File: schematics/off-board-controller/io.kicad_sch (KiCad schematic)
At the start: 6 parts, among them SW5 SW_SPDT_MSM, SW6 SW_Push, SW7 SW_Push, SW8 SW_Push, U7 CA56-12EWA

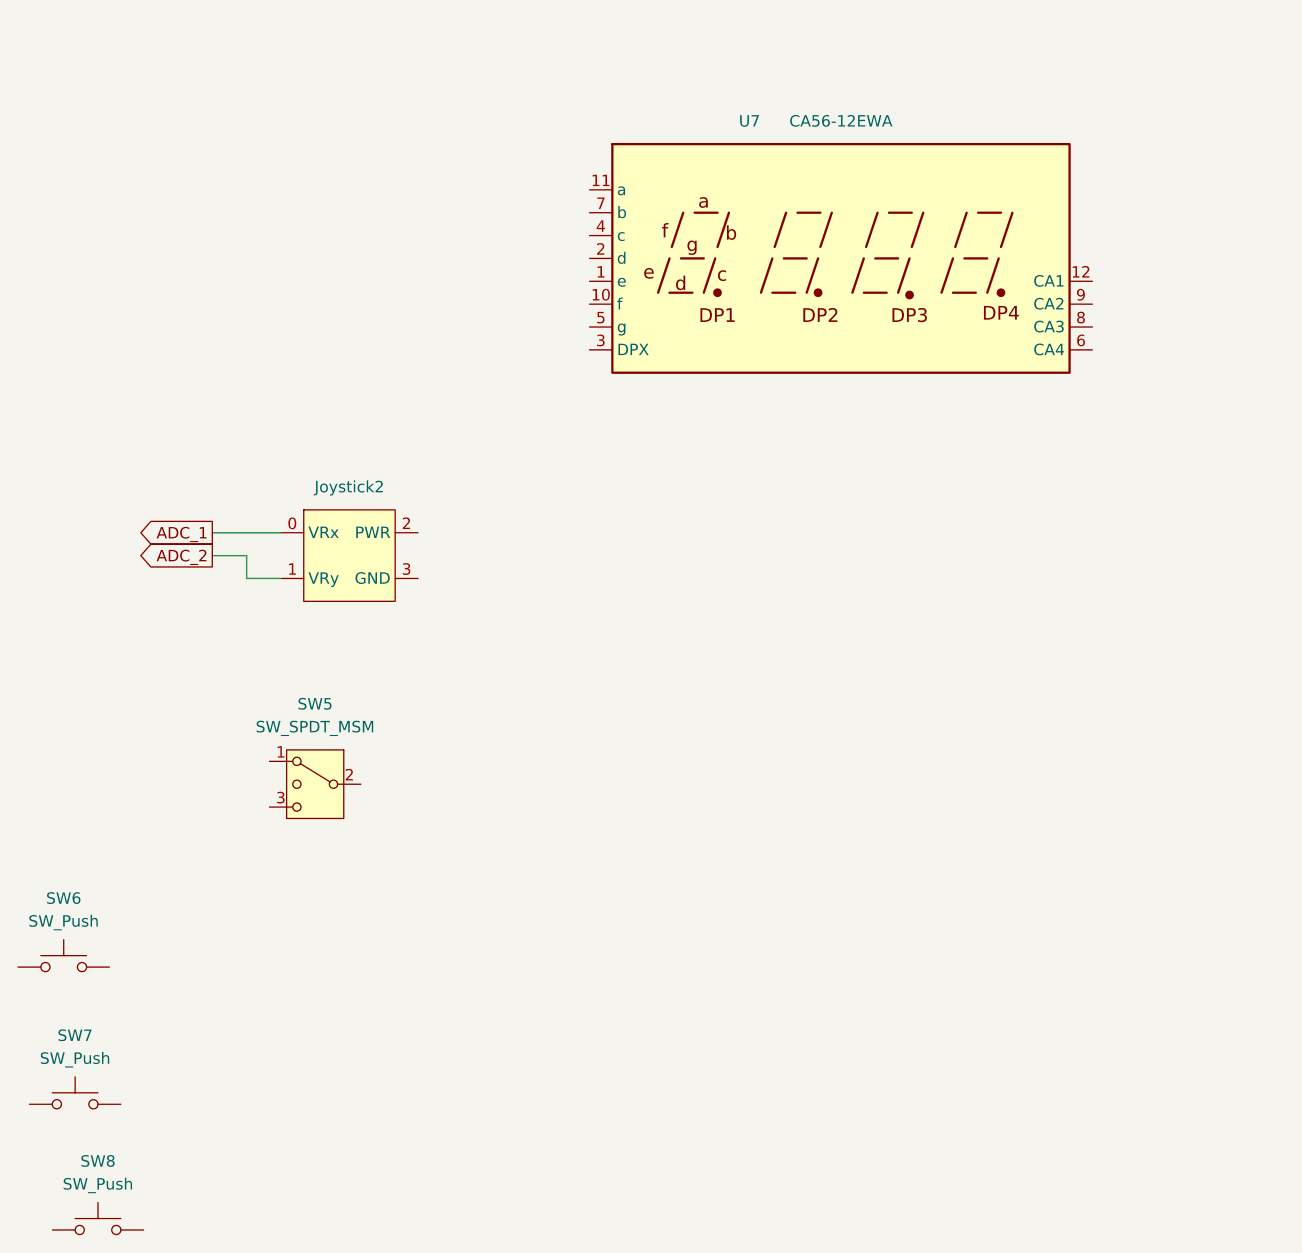
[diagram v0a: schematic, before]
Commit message: off-board: created schematic
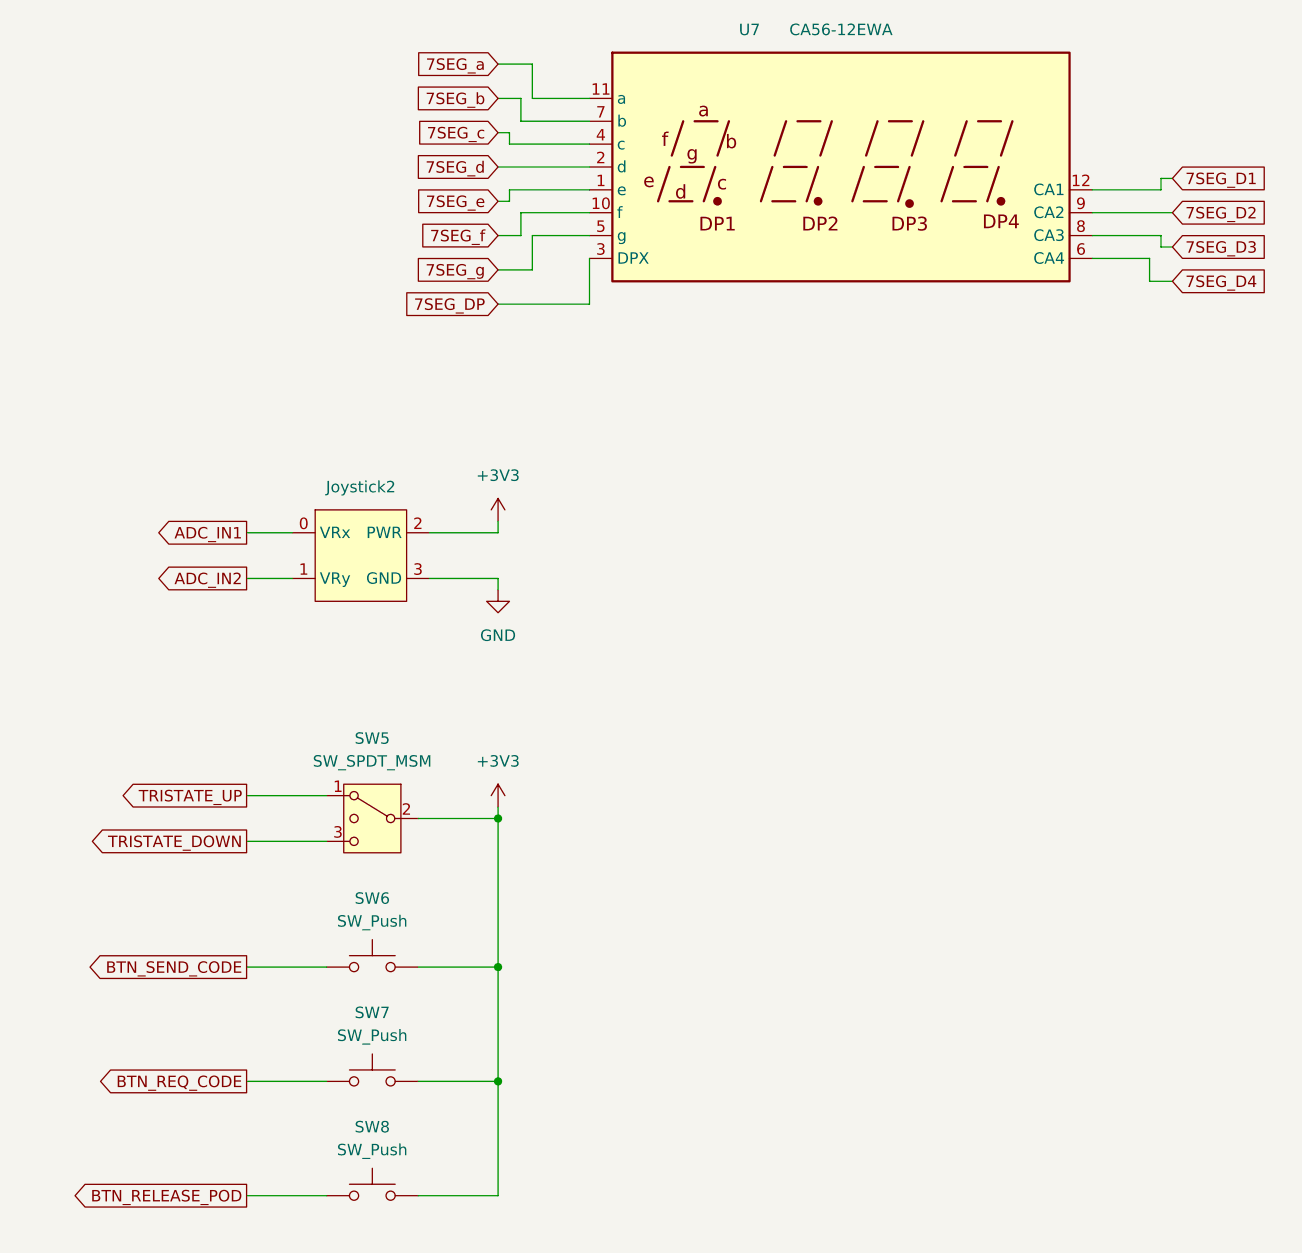
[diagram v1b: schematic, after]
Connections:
- net BTN_REQ_CODE: now reaches SW7.1
- net +3V3: now reaches SW7.2
- net +3V3: now also Joystick2.2 (PWR), SW5.2 (3), SW6.2, SW8.2
- net 7SEG_e: now reaches U7.1 (e)
- net 7SEG_f: now reaches U7.10 (f)
- net 7SEG_a: now reaches U7.11 (a)
- net 7SEG_D1: now reaches U7.12 (CA1)
- net 7SEG_d: now reaches U7.2 (d)
- net 7SEG_DP: now reaches U7.3 (DPX)
- net 7SEG_c: now reaches U7.4 (c)
- net 7SEG_g: now reaches U7.5 (g)
- net 7SEG_D4: now reaches U7.6 (CA4)
- net 7SEG_b: now reaches U7.7 (b)
- net 7SEG_D3: now reaches U7.8 (CA3)
- net 7SEG_D2: now reaches U7.9 (CA2)
- net BTN_RELEASE_POD: now reaches SW8.1
- net TRISTATE_UP: now reaches SW5.1
- net TRISTATE_DOWN: now reaches SW5.3 (4)
- net BTN_SEND_CODE: now reaches SW6.1
- net GND: now reaches Joystick2.3 (GND)
- net ADC_1 renamed ADC_IN1
- net ADC_2 renamed ADC_IN2
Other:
- title: (none) -> Off-board Controller
- moved on the sheet: Joystick2, SW5, SW6, SW7, SW8, U7

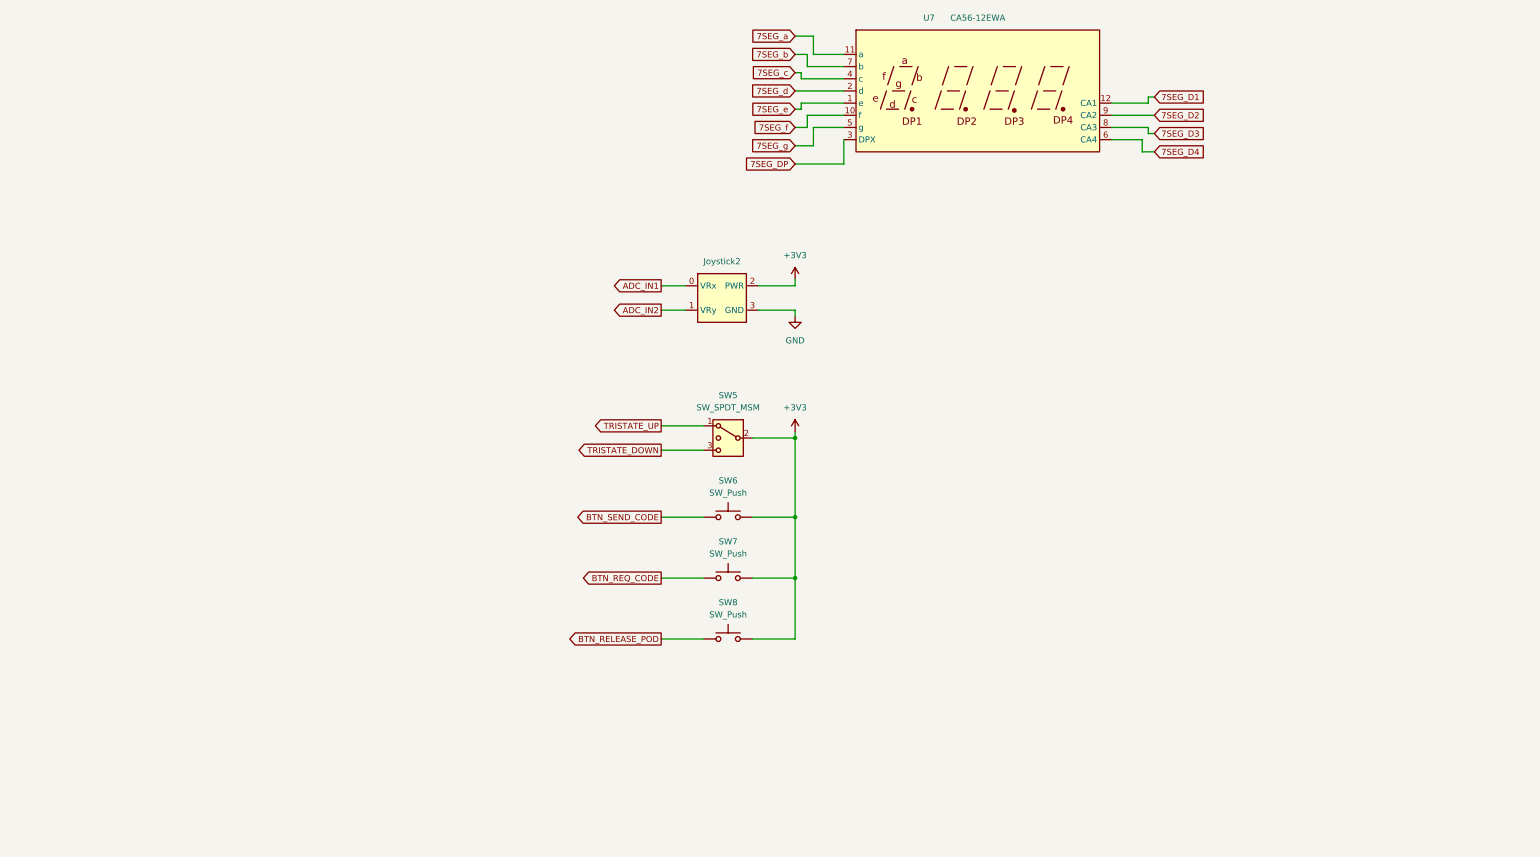
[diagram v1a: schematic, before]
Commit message: finished footprints, schematic, and started layout
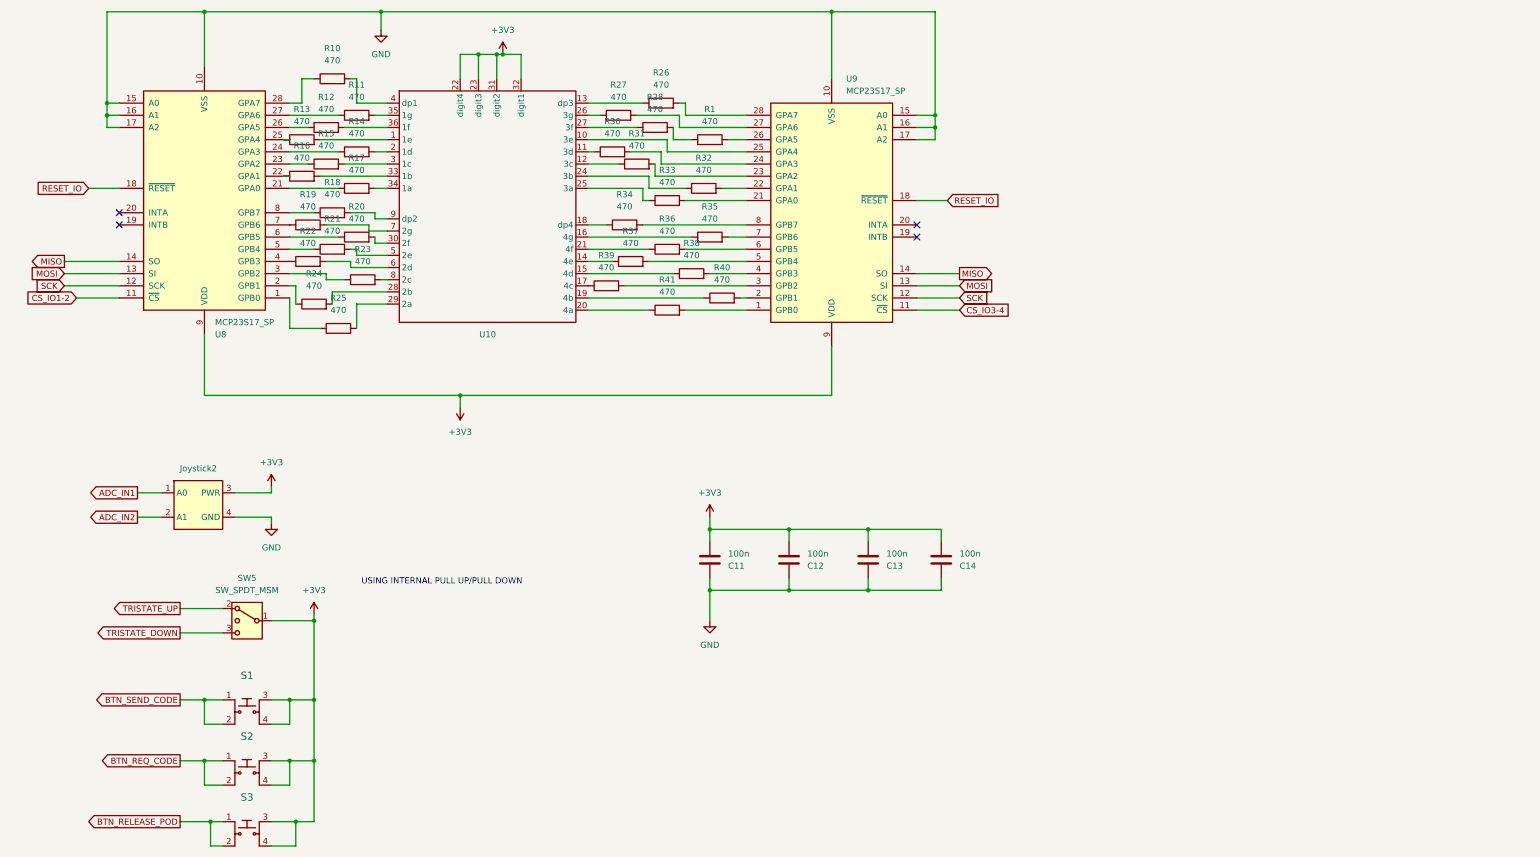
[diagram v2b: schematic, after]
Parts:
- removed SW6, SW7, SW8: SW_Push, symbol Switch:SW_Push
- removed U7: CA56-12EWA, Display_7Segment:CA56-12EWA, symbol Display_Character:CA56-12EWA
- added C11, C12, C13, C14: 100n, Capacitor_SMD:C_0805_2012Metric_Pad1.18x1.45mm_HandSolder, symbol Device:C
- added R1, R10, R11, R12, R13, R14, R15, R16, R17, R18, R19, R20, R21, R22, R23, R24, R25, R26, R27, R28, R30, R31, R32, R33, R34, R35, R36, R37, R38, R39, R40, R41: 470, Resistor_SMD:R_0805_2012Metric_Pad1.20x1.40mm_HandSolder, symbol Device:R
- added S1, S2, S3: ~, sub:button, symbol dk_Tactile-Switches:1825910-6
- added U10: ~, sub:seven_segment, symbol controller:CA56-11SURKWA
- added U8, U9: MCP23S17_SP, Package_DIP:DIP-28_W7.62mm, symbol Interface_Expansion:MCP23S17_SP
- Joystick2: footprint (none) -> Connector:NS-Tech_Grove_1x04_P2mm_Vertical
- SW5: footprint (none) -> sub:spdt
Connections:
- net +3V3: now also Joystick2.3 (PWR), SW5.1 (3), C11.2, C12.2, C13.2, C14.2, S1.3, S1.4, S2.3, S2.4, S3.3, S3.4, U10.22 (digit4), U10.23 (digit3), U10.31 (digit2), U10.32 (digit1), U8.9 (VDD), U9.9 (VDD); no longer Joystick2.2 (PWR), SW5.2 (3)
- net ADC_IN1: now also Joystick2.1 (A0); no longer Joystick2.0 (VRx)
- net ADC_IN2: now also Joystick2.2 (A1); no longer Joystick2.1 (VRy)
- net BTN_RELEASE_POD: now also S3.1, S3.2
- net BTN_REQ_CODE: now also S2.1, S2.2
- net BTN_SEND_CODE: now also S1.1, S1.2
- net GND: now also Joystick2.4 (GND), C11.1, C12.1, C13.1, C14.1, U8.10 (VSS), U8.15 (A0), U8.16 (A1), U8.17 (A2), U9.10 (VSS), U9.15 (A0), U9.16 (A1), U9.17 (A2); no longer Joystick2.3 (GND)
- net TRISTATE_UP: now also SW5.2 (1); no longer SW5.1
- new net: R37.1, U10.14 (4e)
- new net: R37.2, U9.5 (GPB4)
- new net: R41.1, U10.20 (4a)
- new net: R41.2, U9.1 (GPB0)
- new net: R27.1, U10.26 (3g)
- new net: R27.2, U9.27 (GPA6)
- new net: R14.1, U8.24 (GPA3)
- new net: R14.2, U10.2 (1d)
- new net: R36.1, U10.21 (4f)
- new net: R36.2, U9.6 (GPB5)
- new net: R26.1, U10.13 (dp3)
- new net: R26.2, U9.28 (GPA7)
- new net: R11.1, U8.27 (GPA6)
- new net: R11.2, U10.35 (1g)
- new net: R40.1, U10.19 (4b)
- new net: R40.2, U9.2 (GPB1)
- new net: R25.1, U8.1 (GPB0)
- new net: R24.1, U8.2 (GPB1)
- new net: R17.1, U8.21 (GPA0)
- new net: R16.1, U8.22 (GPA1)
- new net: R15.1, U8.23 (GPA2)
- new net: R13.1, U8.25 (GPA4)
- new net: R12.1, U8.26 (GPA5)
- new net: R10.1, U8.28 (GPA7)
- new net: R23.1, U8.3 (GPB2)
- new net: R22.1, U8.4 (GPB3)
- new net: R21.1, U8.5 (GPB4)
- new net: R20.1, U8.6 (GPB5)
- new net: R19.1, U8.7 (GPB6)
- new net: R18.1, U8.8 (GPB7)
- new net: R17.2, U10.34 (1a)
- new net: R10.2, U10.4 (dp1)
- new net: R24.2, U10.28 (2b)
- new net: R21.2, U10.5 (2e)
- new net: R25.2, U10.29 (2a)
- new net: R31.1, U10.12 (3c)
- new net: R31.2, U9.23 (GPA2)
- new net: R23.2, U10.8 (2c)
- new net: R13.2, U10.1 (1e)
- new net: U10.10 (3e), U9.25 (GPA4)
- new net: R30.1, U10.11 (3d)
- new net: R38.1, U10.15 (4d)
- new net: R35.1, U10.16 (4g)
- new net: R39.1, U10.17 (4c)
- new net: R34.1, U10.18 (dp4)
- new net: R32.1, U10.24 (3b)
- new net: R33.1, U10.25 (3a)
- new net: R28.1, U10.27 (3f)
- new net: R15.2, U10.3 (1c)
- new net: R20.2, U10.30 (2f)
- new net: R16.2, U10.33 (1b)
- new net: R12.2, U10.36 (1f)
- new net: R22.2, U10.6 (2d)
- new net: R19.2, U10.7 (2g)
- new net: R18.2, U10.9 (dp2)
- new net: R33.2, U9.21 (GPA0)
- new net: R32.2, U9.22 (GPA1)
- new net: R30.2, U9.24 (GPA3)
- new net: R1.2, U9.26 (GPA5)
- new net: R39.2, U9.3 (GPB2)
- new net: R38.2, U9.4 (GPB3)
- new net: R35.2, U9.7 (GPB6)
- new net: R34.2, U9.8 (GPB7)
- new net: R1.1, R28.2
- new net CS_IO1-2: U8.11 (~{CS})
- new net CS_IO3-4: U9.11 (~{CS})
- new net MISO: U8.14 (SO), U9.14 (SO)
- new net MOSI: U8.13 (SI), U9.13 (SI)
- new net RESET_IO: U8.18 (~{RESET}), U9.18 (~{RESET})
- new net SCK: U8.12 (SCK), U9.12 (SCK)
- no-connect marks 0 -> 4
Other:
- note added: "USING INTERNAL PULL UP/PULL DOWN"
- moved on the sheet: Joystick2, SW5

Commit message: layout
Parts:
- removed R28: 470, Resistor_SMD:R_0805_2012Metric_Pad1.20x1.40mm_HandSolder, symbol Device:R
- added R2: 470, Resistor_SMD:R_0805_2012Metric_Pad1.20x1.40mm_HandSolder, symbol Device:R
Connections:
- net at U10.10 (3e): now also R2.1; no longer U9.25 (GPA4)
- net at U10.27 (3f): now also R1.1
- new net: R2.2, U9.25 (GPA4)
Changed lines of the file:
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@@
 	(wire
 		(pts
-			(xy 147.32 45.72) (xy 137.16 45.72)
+			(xy 137.16 45.72) (xy 154.94 45.72)
 		)
 		(stroke
@@
 	(wire
 		(pts
-			(xy 137.16 48.26) (xy 153.67 48.26)
+			(xy 137.16 48.26) (xy 146.05 48.26)
 		)
 		(stroke
@@
 	(symbol
 		(lib_id "Device:R")
+		(at 149.86 48.26 90)
+		(unit 1)
+		(exclude_from_sim no)
+		(in_bom yes)
+		(on_board yes)
+		(dnp no)
+		(fields_autoplaced yes)
+		(property "Reference" "R2"
+			(at 149.86 41.91 90)
+			(effects
+				(font
+					(size 1.27 1.27)
+				)
+			)
+		)
+		(property "Value" "470"
+			(at 149.86 44.45 90)
+			(effects
+				(font
+					(size 1.27 1.27)
+				)
+			)
+		)
+		(property "Footprint" "Resistor_SMD:R_0805_2012Metric_Pad1.20x1.40mm_HandSolder"
+			(at 149.86 50.038 90)
+			(effects
+				(font
+					(size 1.27 1.27)
+				)
+				(hide yes)
+			)
+		)
+		(property "Datasheet" "~"
+			(at 149.86 48.26 0)
+			(effects
+				(font
+					(size 1.27 1.27)
+				)
+				(hide yes)
+			)
+		)
+		(property "Description" "Resistor"
+			(at 149.86 48.26 0)
+			(effects
+				(font
+					(size 1.27 1.27)
+				)
+				(hide yes)
+			)
+		)
+		(pin "2"
+		)
+		(pin "1"
+		)
+		(instances
+			(project "controller"
+				(path "/0775f04a-8a0e-41f5-b442-dacb2efdb863/92c85f3a-14b3-4661-ad21-779315976c0e"
+					(reference "R2")
+					(unit 1)
+				)
+			)
+		)
+	)
+	(symbol
+		(lib_id "Device:R")
 		(at 144.78 66.04 90)
 		(unit 1)
@@
 					(unit 1)
 				)
-			)
-		)
-	)
-	(symbol
-		(lib_id "Device:R")
-		(at 151.13 45.72 90)
-		(unit 1)
-		(exclude_from_sim no)
-		(in_bom yes)
-		(on_board yes)
-		(dnp no)
-		(fields_autoplaced yes)
-		(property "Reference" "R28"
-			(at 151.13 39.37 90)
-			(effects
-				(font
-					(size 1.27 1.27)
-				)
-			)
-		)
-		(property "Value" "470"
-			(at 151.13 41.91 90)
-			(effects
-				(font
-					(size 1.27 1.27)
-				)
-			)
-		)
-		(property "Footprint" "Resistor_SMD:R_0805_2012Metric_Pad1.20x1.40mm_HandSolder"
-			(at 151.13 47.498 90)
-			(effects
-				(font
-					(size 1.27 1.27)
-				)
-				(hide yes)
-			)
-		)
-		(property "Datasheet" "~"
-			(at 151.13 45.72 0)
-			(effects
-				(font
-					(size 1.27 1.27)
-				)
-				(hide yes)
-			)
-		)
-		(property "Description" "Resistor"
-			(at 151.13 45.72 0)
-			(effects
-				(font
-					(size 1.27 1.27)
-				)
-				(hide yes)
-			)
-		)
-		(pin "2"
-		)
-		(pin "1"
-		)
-		(instances
-			(project "controller"
-				(path "/0775f04a-8a0e-41f5-b442-dacb2efdb863/92c85f3a-14b3-4661-ad21-779315976c0e"
-					(reference "R28")
-					(unit 1)
-				)
